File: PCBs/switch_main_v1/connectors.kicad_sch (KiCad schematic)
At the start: 4 parts, among them IC1101 MPQ5850GJ-AEC1-Z, J1101 76825-0004, U1101 TVS2701DRBR

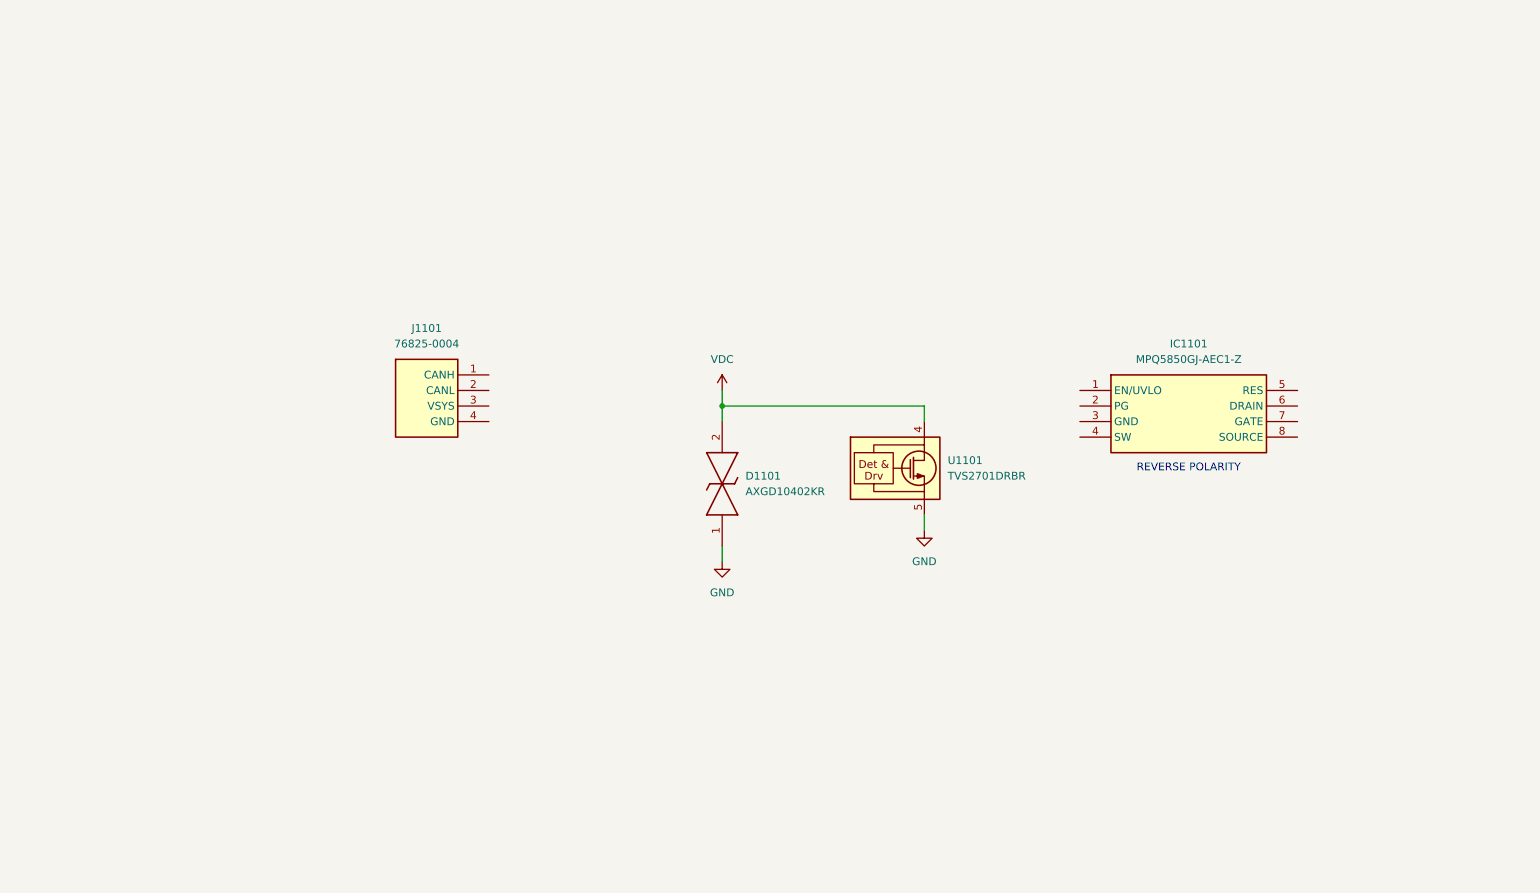
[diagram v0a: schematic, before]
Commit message: Connectors schematic almost complete
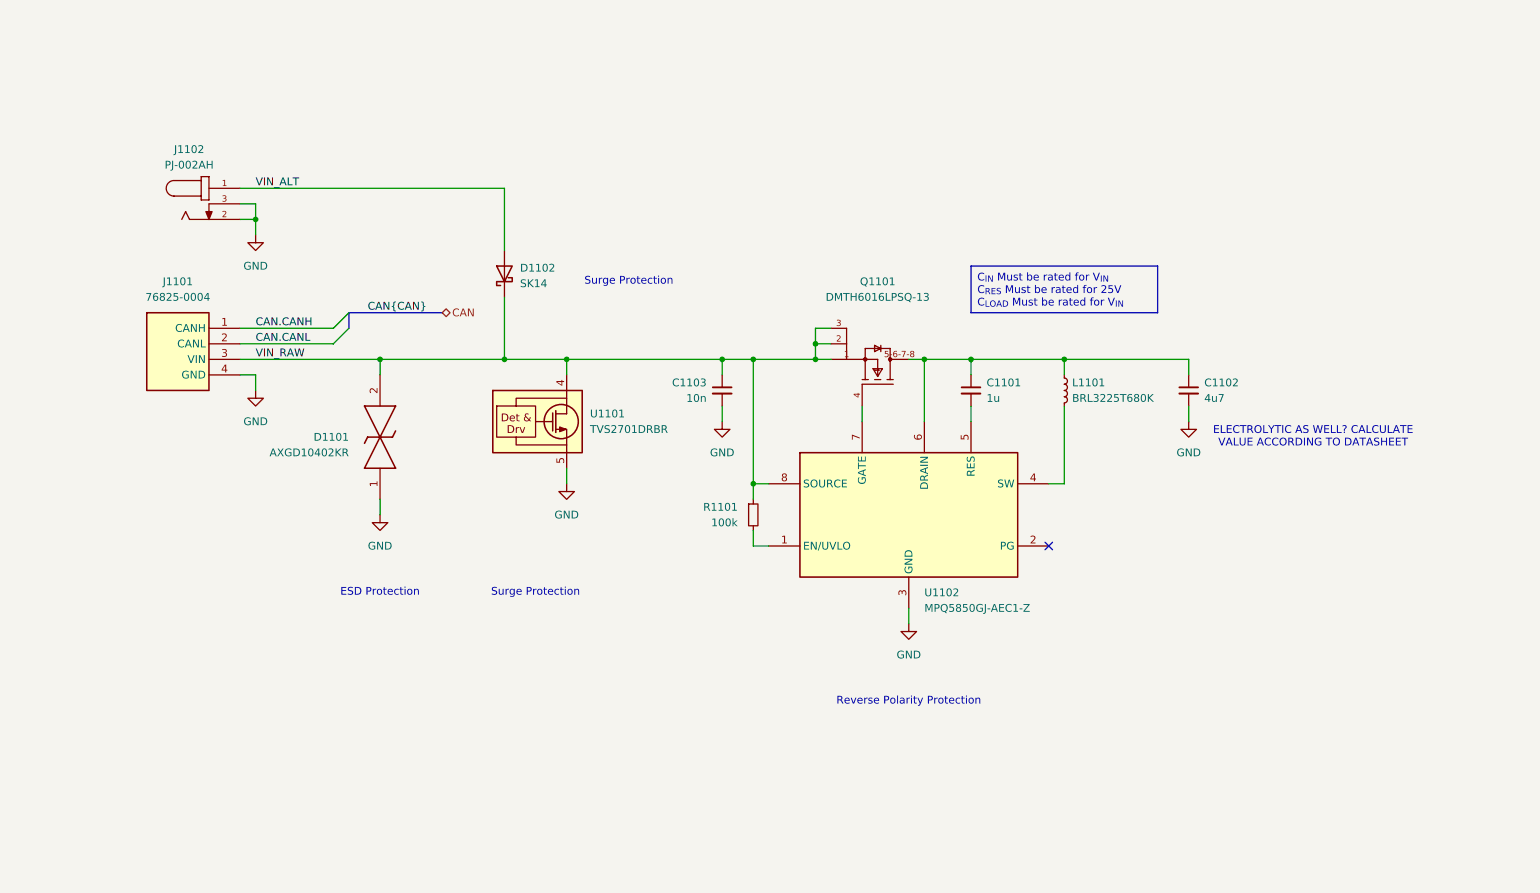
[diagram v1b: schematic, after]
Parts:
- removed IC1101: MPQ5850GJ-AEC1-Z, SOT65P280X100-8N, symbol MPQ5850GJ-AEC1-Z:MPQ5850GJ-AEC1-Z
- added C1101: 1u, Capacitor_SMD:C_0402_1005Metric, symbol Device:C_Small
- added C1102: 4u7, Capacitor_SMD:C_0402_1005Metric, symbol Device:C_Small
- added C1103: 10n, Capacitor_SMD:C_0402_1005Metric, symbol Device:C_Small
- added D1102: SK14, Diode_SMD:D_SMA, symbol Device:D_Schottky
- added J1102: PJ-002AH, switch_footprints:CUI_PJ-002AH, symbol PJ-002AH:PJ-002AH
- added L1101: BRL3225T680K, Inductor_SMD:L_1210_3225Metric, symbol Device:L_Small
- added Q1101: DMTH6016LPSQ-13, switch_footprints:Diodes_Incorporated-PowerDI5060-8-03_2017-0-MFG, symbol DMTH6016LPSQ-13:DMTH6016LPSQ-13
- added R1101: 100k, Resistor_SMD:R_0402_1005Metric, symbol Device:R_Small
- added U1102: MPQ5850GJ-AEC1-Z, SOT65P280X100-8N, symbol MPQ5850GJ-AEC1-Z:MPQ5850GJ-AEC1-Z
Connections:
- net VDC is gone; now on net VIN_RAW: D1101.2, U1101.1 (IN), U1101.2 (IN), U1101.3 (IN), U1101.4 (IN)
- net GND: now also J1101.4 (GND), C1102.2, C1103.2, J1102.2, J1102.3, U1102.3 (GND)
- net CAN.CANH: now reaches J1101.1 (CANH)
- net CAN.CANL: now reaches J1101.2 (CANL)
- net VIN_RAW: now reaches J1101.3 (VIN)
- net VIN_RAW: now also C1103.1, D1102.1 (K), Q1101.1 (S), Q1101.2 (S), Q1101.3 (S), R1101.1, U1102.8 (SOURCE)
- new net: C1101.1, C1102.1, L1101.1, Q1101.5-6-7-8 (D), U1102.6 (DRAIN)
- new net: L1101.2, U1102.4 (SW)
- new net: C1101.2, U1102.5 (RES)
- new net: R1101.2, U1102.1 (EN/UVLO)
- new net: Q1101.4 (G), U1102.7 (GATE)
- new net VIN_ALT: D1102.2 (A), J1102.1
- no-connect marks 0 -> 1
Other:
- note added: "ELECTROLYTIC AS WELL? CALCULATE VALUE ACCORDING TO DATASHEET"
- note added: "ESD Protection"
- note added: "Reverse Polarity Protection"
- note added: "Surge Protection"
- note removed: "REVERSE POLARITY"
- moved on the sheet: D1101, J1101, U1101

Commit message: Added schematic annotations
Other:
- note added: "DEBUG CONNECTOR"
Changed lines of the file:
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@@
+		)
+	)
+	(text "DEBUG CONNECTOR"
+		(exclude_from_sim no)
+		(at 63.5 144.78 0)
+		(effects
+			(font
+				(size 1.27 1.27)
+			)
 		)
 	)

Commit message: Schematic progress
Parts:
- added J1103: Conn_ST_STDC14, symbol Connector:Conn_ST_STDC14
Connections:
- net GND: now also J1103.5 (GND), J1103.7 (GND)
- new net +2V5: J1103.3 (VCC)
- no-connect marks 1 -> 3
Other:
- note removed: "DEBUG CONNECTOR"
- moved on the sheet: C1101, C1102, C1103, D1101, D1102, J1101, J1102, L1101, Q1101, R1101, U1101, U1102

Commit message: GbE part of schematic done
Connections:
- net RST: now reaches J1103.12 (~{RST})
- net UART.RX: now reaches J1103.13 (VCP_RX)
- net UART.TX: now reaches J1103.14 (VCP_TX)
- net SWD.SWDIO: now reaches J1103.4 (JTMS/SWDIO)
- net SWD.SWCLK: now reaches J1103.6 (JCLK/SWCLK)
- net SWD.SWO: now reaches J1103.8 (JTDO/SWO)
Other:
- company: (none) -> Ben Smith

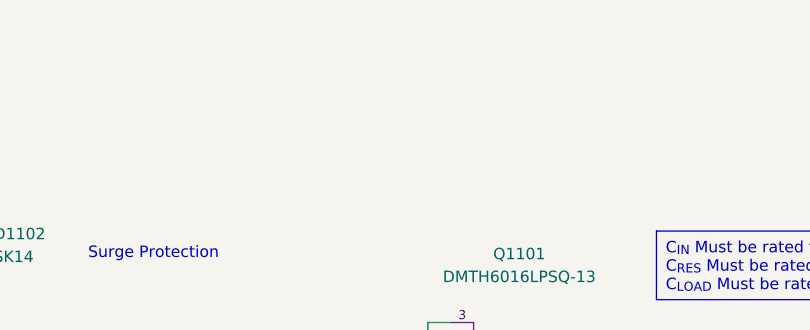
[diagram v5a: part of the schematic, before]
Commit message: Common mode choke needed on power input
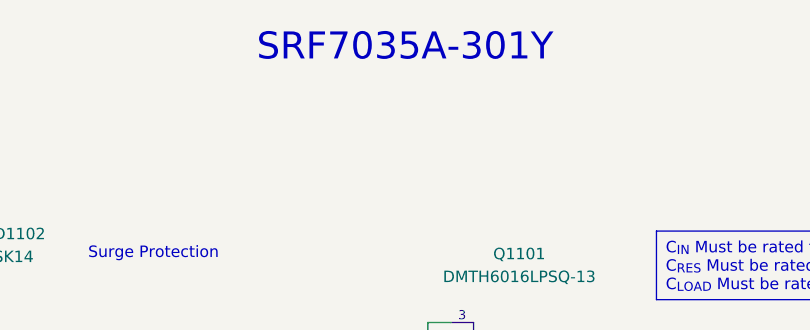
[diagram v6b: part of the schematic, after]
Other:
- note added: "SRF7035A-301Y"
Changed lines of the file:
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@@
+		)
+	)
+	(text "SRF7035A-301Y"
+		(exclude_from_sim no)
+		(at 160.02 35.56 0)
+		(effects
+			(font
+				(size 3 3)
+			)
 		)
 	)
@@
 	(label "UART.TX"
 		(at 78.74 154.94 0)
+		(fields_autoplaced yes)
 		(effects
 			(font
@@
 	(label "UART.RX"
 		(at 78.74 152.4 0)
+		(fields_autoplaced yes)
 		(effects
 			(font

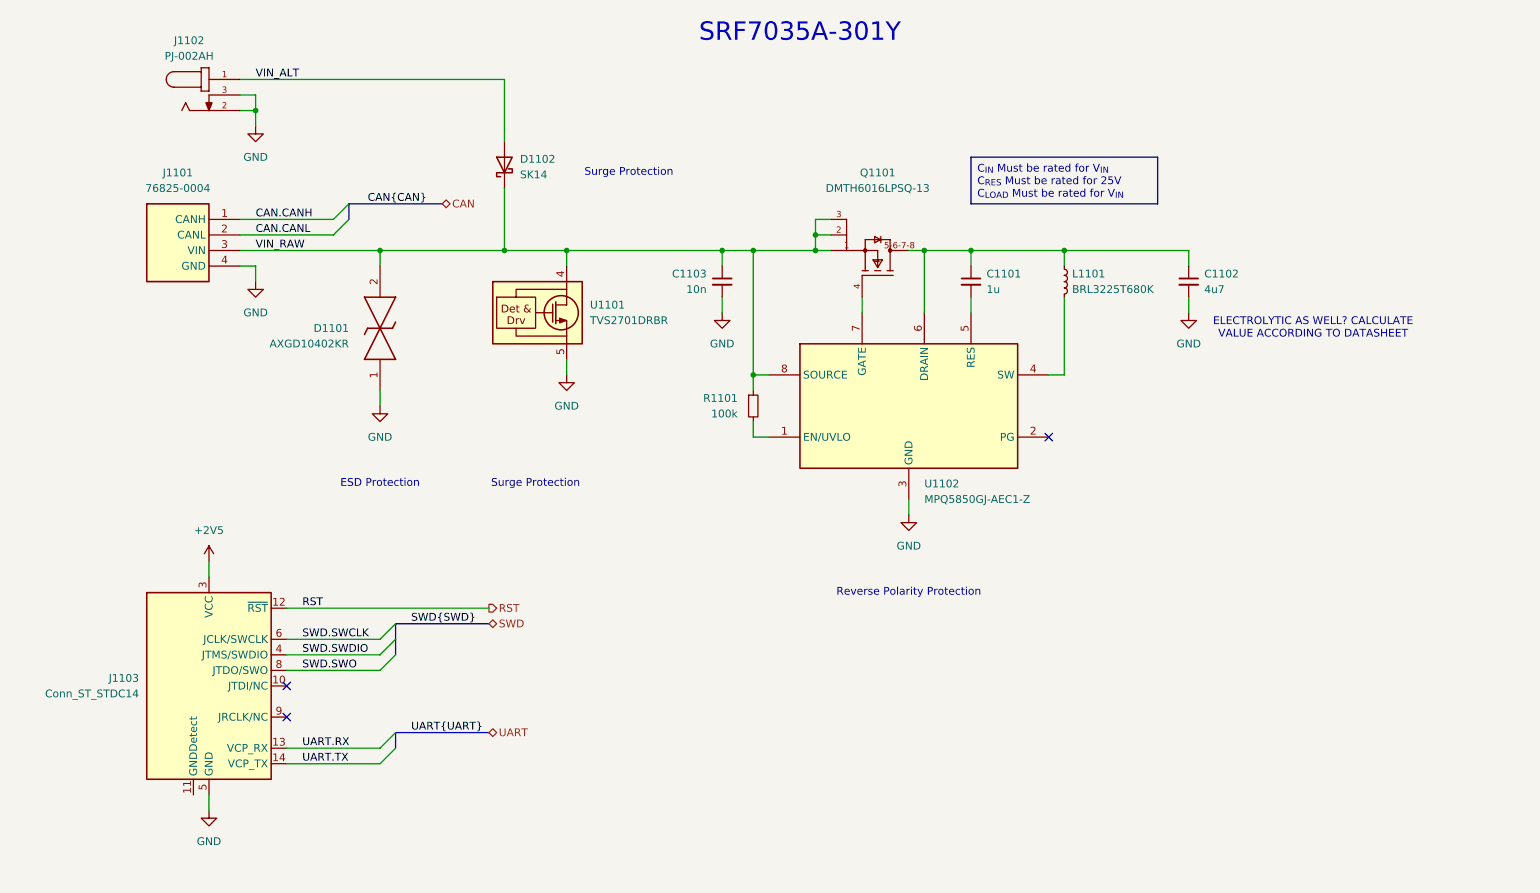
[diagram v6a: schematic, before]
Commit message: Progress on CAN schematic sheet
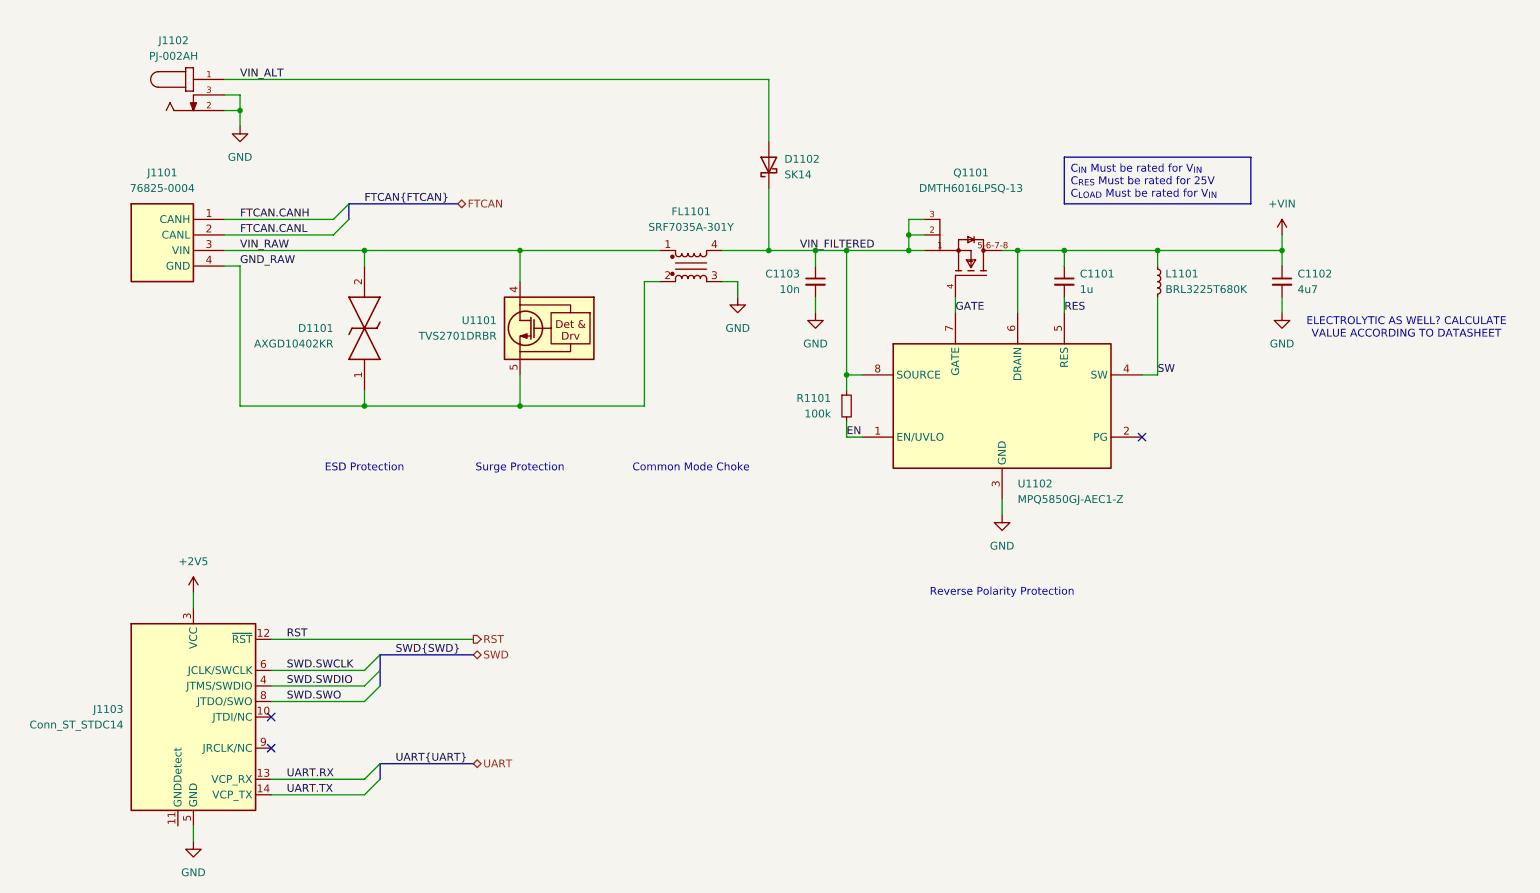
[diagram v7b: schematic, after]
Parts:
- added FL1101: SRF7035A-301Y, switch_footprints:SRF7035A301Y, symbol SRF7035A-301Y:SRF7035A-301Y
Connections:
- net GND: now also FL1101.3; no longer D1101.1, J1101.4 (GND), U1101.5 (GND), U1101.6 (GND), U1101.7 (GND), U1101.8 (GND)
- net VIN_RAW: now also FL1101.1; no longer C1103.1, D1102.1 (K), Q1101.1 (S), Q1101.2 (S), Q1101.3 (S), R1101.1, U1102.8 (SOURCE)
- net +VIN: now reaches C1101.1, C1102.1, L1101.1, Q1101.5-6-7-8 (D), U1102.6 (DRAIN)
- net SW: now reaches L1101.2, U1102.4 (SW)
- net RES: now reaches C1101.2, U1102.5 (RES)
- net EN: now reaches R1101.2, U1102.1 (EN/UVLO)
- net GATE: now reaches Q1101.4 (G), U1102.7 (GATE)
- net CAN.CANH renamed FTCAN.CANH
- net CAN.CANL renamed FTCAN.CANL
- new net GND_RAW: D1101.1, FL1101.2, J1101.4 (GND), U1101.5 (GND), U1101.6 (GND), U1101.7 (GND), U1101.8 (GND)
- new net VIN_FILTERED: C1103.1, D1102.1 (K), FL1101.4, Q1101.1 (S), Q1101.2 (S), Q1101.3 (S), R1101.1, U1102.8 (SOURCE)
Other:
- note added: "Common Mode Choke"
- note removed: "SRF7035A-301Y"
- moved on the sheet: C1101, C1102, C1103, D1101, J1101, J1102, J1103, L1101, Q1101, R1101, U1101, U1102

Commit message: Changed MCU to STM32H573VIT3Q
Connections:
- net +VIN renamed VIN_PROTECTED
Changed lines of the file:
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@@
-	(wire
-		(pts
-			(xy 238.76 68.58) (xy 238.76 71.12)
-		)
-		(stroke
-			(width 0)
-			(type default)
-		)
-	)
 	(wire
 		(pts
@@
 		(pts
 			(xy 167.64 91.44) (xy 167.64 93.98)
+		)
+		(stroke
+			(width 0)
+			(type default)
+		)
+	)
+	(wire
+		(pts
+			(xy 238.76 71.12) (xy 243.84 71.12)
 		)
 		(stroke
@@
 		(shape bidirectional)
 		(at 106.68 137.16 0)
+		(fields_autoplaced yes)
+		(effects
+			(font
+				(size 1.27 1.27)
+			)
+			(justify left)
+		)
+	)
+	(hierarchical_label "VIN_PROTECTED"
+		(shape output)
+		(at 243.84 71.12 0)
 		(fields_autoplaced yes)
 		(effects
@@
 					(unit 1)
 				)
-			)
-		)
-	)
-	(symbol
-		(lib_id "power:+5V")
-		(at 238.76 68.58 0)
-		(unit 1)
-		(exclude_from_sim no)
-		(in_bom yes)
-		(on_board yes)
-		(dnp no)
-		(fields_autoplaced yes)
-		(property "Reference" "#PWR01102"
-			(at 238.76 72.39 0)
-			(effects
-				(font
-					(size 1.27 1.27)
-				)
-				(hide yes)
-			)
-		)
-		(property "Value" "+VIN"
-			(at 238.76 63.5 0)
-			(effects
-				(font
-					(size 1.27 1.27)
-				)
-			)
-		)
-		(property "Footprint" ""
-			(at 238.76 68.58 0)
-			(effects
-				(font
-					(size 1.27 1.27)
-				)
-				(hide yes)
-			)
-		)
-		(property "Datasheet" ""
-			(at 238.76 68.58 0)
-			(effects
-				(font
-					(size 1.27 1.27)
-				)
-				(hide yes)
-			)
-		)
-		(property "Description" "Power symbol creates a global label with name \"+VIN\""
-			(at 238.76 68.58 0)
-			(effects
-				(font
-					(size 1.27 1.27)
-				)
-				(hide yes)
-			)
-		)
-		(pin "1"
-		)
-		(instances
-			(project "switch_main_v1"
-				(path "/4638d344-96ef-43ce-a37a-2df37185796e/c12353f3-756b-4e5c-881f-05c4e6fe5abb"
-					(reference "#PWR01102")
-					(unit 1)
-				)
